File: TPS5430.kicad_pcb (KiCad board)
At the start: 2 copper layers, 55 x 20 mm, 36 parts, among them J1 Barrel_Jack, J2 Screw_Terminal_01x02, Q1 AO3401A, U1 TPS5430DDA

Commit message: Add library with used extra parts
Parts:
- J1: footprint MyFootprints:DC-005-5A-2.0-SMT -> tps5430:DC-005-5A-2.0-SMT
- L1: footprint MyFootprints:L_Sunlord_MWSA1004S_10x11.5x4mm -> tps5430:L_Sunlord_MWSA1004S_10x11.5x4mm
- REF** (x3): footprint MyFootprints:ToolingHole_1.152mm -> tps5430:ToolingHole_1.152mm
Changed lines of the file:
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@@
     )
   )
-  (footprint "MyFootprints:L_Sunlord_MWSA1004S_10x11.5x4mm" (layer "F.Cu")
+  (footprint "tps5430:L_Sunlord_MWSA1004S_10x11.5x4mm" (layer "F.Cu")
     (at 187.4 87.1 90)
     (descr "Inductor, Sunlord, MWSA series, MWSA1004S-470MT, SMD_10x11.5x4.0mm, 47uH ±20% 3.3A 145mΩ SMD,10x11.5x4.0mm Power Inductors RoHS, https://datasheet.lcsc.com/szlcsc/1912111437_Sunlord-MWSA1004S-470MT_C408491.pdf")
@@
     (property "Sheetname" "")
     (attr smd)
-    (fp_text reference "L1" (at -6.3 6 90) (layer "F.SilkS")
-      (effects (font (size 1 1) (thickness 0.15)))
-    )
-    (fp_text value "47u" (at 16.75 -21.8 90) (layer "F.Fab")
+    (fp_text reference "L1" (at 0 -6.25 90) (layer "F.SilkS")
+      (effects (font (size 1 1) (thickness 0.15)))
+    )
+    (fp_text value "47u" (at 0 6.5 90) (layer "F.Fab")
       (effects (font (size 1 1) (thickness 0.15)))
     )
@@
     (fp_line (start -5.15 5.3) (end 5.15 5.3) (layer "F.SilkS") (width 0.12))
     (fp_line (start -5.15 -5.3) (end 5.15 -5.3) (layer "F.SilkS") (width 0.12))
-    (fp_line (start 6.95 -5.3) (end -6.95 -5.3) (layer "F.CrtYd") (width 0.05))
+    (fp_line (start -6.95 5.3) (end 6.95 5.3) (layer "F.CrtYd") (width 0.05))
     (fp_line (start -6.95 -5.3) (end -6.95 5.3) (layer "F.CrtYd") (width 0.05))
     (fp_line (start 6.95 5.3) (end 6.95 -5.3) (layer "F.CrtYd") (width 0.05))
-    (fp_line (start -6.95 5.3) (end 6.95 5.3) (layer "F.CrtYd") (width 0.05))
+    (fp_line (start 6.95 -5.3) (end -6.95 -5.3) (layer "F.CrtYd") (width 0.05))
+    (fp_line (start 5.75 5) (end 5.75 -5) (layer "F.Fab") (width 0.1))
+    (fp_line (start -5.75 -5) (end -5.75 5) (layer "F.Fab") (width 0.1))
     (fp_line (start 5.75 -5) (end -5.75 -5) (layer "F.Fab") (width 0.1))
     (fp_line (start -5.75 5) (end 5.75 5) (layer "F.Fab") (width 0.1))
-    (fp_line (start 5.75 5) (end 5.75 -5) (layer "F.Fab") (width 0.1))
-    (fp_line (start -5.75 -5) (end -5.75 5) (layer "F.Fab") (width 0.1))
     (pad "1" smd rect locked (at -4.75 0 90) (size 4.1 4.1) (layers "F.Cu" "F.Paste" "F.Mask" "Eco2.User")
       (net 5 "Net-(C6-Pad2)") (pinfunction "1") (pintype "passive"))
     (pad "2" smd rect locked (at 4.75 0 90) (size 4.1 4.1) (layers "F.Cu" "F.Paste" "F.Mask")
       (net 6 "VDD") (pinfunction "2") (pintype "passive"))
-    (model "${KICAD_USER_3DMODEL_DIR}/MWSA1004S-150MT.stp"
+    (model "${KIPRJMOD}/lib/3dmodels/MWSA1004S-150MT.stp"
       (offset (xyz 0 0 0))
       (scale (xyz 1 1 1))
@@
     )
   )
-  (footprint "MyFootprints:ToolingHole_1.152mm" (layer "F.Cu")
+  (footprint "tps5430:ToolingHole_1.152mm" (layer "F.Cu")
     (at 152.75 77.5)
     (descr "Mounting Hole 1.152mm, no annular")
@@
     (pad "1" np_thru_hole circle locked (at 0 0) (size 2.2 2.2) (drill 2.2) (layers *.Cu *.Mask))
   )
-  (footprint "MyFootprints:ToolingHole_1.152mm" (layer "F.Cu")
+  (footprint "tps5430:ToolingHole_1.152mm" (layer "F.Cu")
     (at 196.25 77.5)
     (descr "Mounting Hole 1.152mm, no annular")
@@
     )
   )
-  (footprint "MyFootprints:ToolingHole_1.152mm" (layer "F.Cu")
+  (footprint "tps5430:ToolingHole_1.152mm" (layer "F.Cu")
     (at 196.25 94.5)
     (descr "Mounting Hole 1.152mm, no annular")
@@
     )
   )
-  (footprint "MyFootprints:DC-005-5A-2.0-SMT" (layer "F.Cu")
+  (footprint "tps5430:DC-005-5A-2.0-SMT" (layer "F.Cu")
     (at 154.3 86)
     (descr "XKB Barrel Jack Connector, 2.5A, 2.0mm pin, 2.1mm/5.5mm plug, DC-005-5A-2.0-SMT-1, https://datasheet.lcsc.com/szlcsc/1810291122_XKB-Connectivity-DC-005-5A-2-0-SMT_C319134.pdf")
@@
     (property "Sheetfile" "TPS5430.kicad_sch")
     (property "Sheetname" "")
-    (fp_text reference "J1" (at 6.7 -8.5) (layer "F.SilkS")
+    (fp_text reference "J1" (at 0 0) (layer "F.SilkS")
       (effects (font (size 1.27 1.27) (thickness 0.254)))
     )
@@
       (effects (font (size 1.27 1.27) (thickness 0.254)))
     )
-    (fp_line (start 7.4 4.5) (end 6.1 4.5) (layer "F.SilkS") (width 0.1))
+    (fp_line (start -4.15 4.56) (end -4.15 -4.56) (layer "F.SilkS") (width 0.12))
+    (fp_line (start 6.1 -4.5) (end 7.4 -4.5) (layer "F.SilkS") (width 0.1))
+    (fp_line (start -4.15 -3) (end 0.65 -3) (layer "F.SilkS") (width 0.12))
     (fp_line (start -7.4 -4.5) (end -7.4 4.5) (layer "F.SilkS") (width 0.1))
-    (fp_line (start -4.15 -3) (end 0.65 -3) (layer "F.SilkS") (width 0.12))
-    (fp_line (start -0.4 4.5) (end 1.6 4.5) (layer "F.SilkS") (width 0.1))
-    (fp_line (start -4.15 4.56) (end -4.15 -4.56) (layer "F.SilkS") (width 0.12))
-    (fp_line (start -0.4 -4.5) (end 1.6 -4.5) (layer "F.SilkS") (width 0.1))
-    (fp_line (start 6.1 -4.5) (end 7.4 -4.5) (layer "F.SilkS") (width 0.1))
-    (fp_line (start -7.4 4.5) (end -4.9 4.5) (layer "F.SilkS") (width 0.1))
-    (fp_line (start 7.4 -4.5) (end 7.4 4.5) (layer "F.SilkS") (width 0.1))
     (fp_line (start -4.15 3) (end 0.65 3) (layer "F.SilkS") (width 0.12))
     (fp_line (start -4.9 -4.5) (end -7.4 -4.5) (layer "F.SilkS") (width 0.1))
+    (fp_line (start 7.4 4.5) (end 6.1 4.5) (layer "F.SilkS") (width 0.1))
+    (fp_line (start -0.4 -4.5) (end 1.6 -4.5) (layer "F.SilkS") (width 0.1))
+    (fp_line (start 7.4 -4.5) (end 7.4 4.5) (layer "F.SilkS") (width 0.1))
+    (fp_line (start -7.4 4.5) (end -4.9 4.5) (layer "F.SilkS") (width 0.1))
+    (fp_line (start -0.4 4.5) (end 1.6 4.5) (layer "F.SilkS") (width 0.1))
     (fp_arc (start 0.65 0) (end 0.65 3) (angle -180) (layer "F.SilkS") (width 0.12))
     (fp_line (start 7.9 7.4) (end -7.9 7.4) (layer "F.CrtYd") (width 0.1))
     (fp_line (start -7.9 -7.4) (end 7.9 -7.4) (layer "F.CrtYd") (width 0.1))
+    (fp_line (start 7.9 -7.4) (end 7.9 7.4) (layer "F.CrtYd") (width 0.1))
     (fp_line (start -7.9 7.4) (end -7.9 -7.4) (layer "F.CrtYd") (width 0.1))
-    (fp_line (start 7.9 -7.4) (end 7.9 7.4) (layer "F.CrtYd") (width 0.1))
+    (fp_line (start 7.4 4.5) (end -7.4 4.5) (layer "F.Fab") (width 0.2))
     (fp_line (start 7.4 -4.5) (end 7.4 4.5) (layer "F.Fab") (width 0.2))
+    (fp_line (start -7.4 -4.5) (end 7.4 -4.5) (layer "F.Fab") (width 0.2))
     (fp_line (start -7.4 4.5) (end -7.4 -4.5) (layer "F.Fab") (width 0.2))
-    (fp_line (start -7.4 -4.5) (end 7.4 -4.5) (layer "F.Fab") (width 0.2))
-    (fp_line (start 7.4 4.5) (end -7.4 4.5) (layer "F.Fab") (width 0.2))
     (pad "1" smd rect (at 3.7 -5.7 90) (size 2.4 2.8) (layers "F.Cu" "F.Paste" "F.Mask")
       (net 8 "Net-(F1-Pad1)") (pintype "passive"))
@@
     (pad "MH1" np_thru_hole circle (at -2.4 0) (size 1.6 1.6) (drill 1.6) (layers *.Cu *.Mask))
     (pad "MH2" np_thru_hole circle (at 2.1 0) (size 1.8 1.8) (drill 1.8) (layers *.Cu *.Mask))
-    (model "${KICAD_USER_3DMODEL_DIR}/DC-005-5A-2.0-SMT.stp"
-      (offset (xyz 0 0 0))
-      (scale (xyz 1 1 1))
+    (model "${KIPRJMOD}/lib/3dmodels/DC-005-5A-2.0-SMT.stp"
+      (offset (xyz 0 0 0))
+      (scale (xyz 1 1 1))

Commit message: Add License notice in files and on the PCB
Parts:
- added LOGO1: Logo_Open_Hardware_Small, Symbol:OSHW-Logo_11.4x12mm_Copper, B.Cu at (154.8, 86.0)
- added REF**: KiCad-Logo2_5mm_Copper, Symbol:KiCad-Logo2_5mm_Copper, B.Cu at (191.5, 86.0)
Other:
- board text added: "git.io/JWgnY"

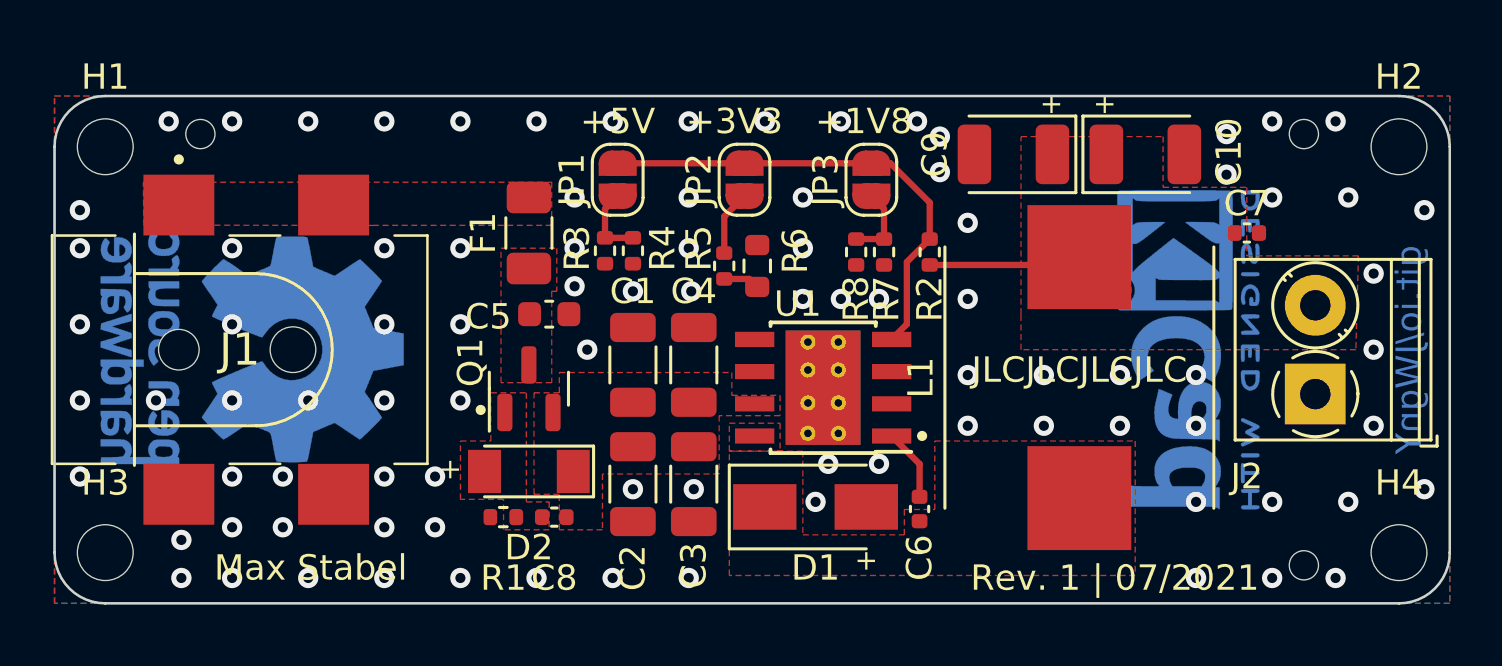
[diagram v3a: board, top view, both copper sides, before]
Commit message: Add TP & 12V SolderJumper
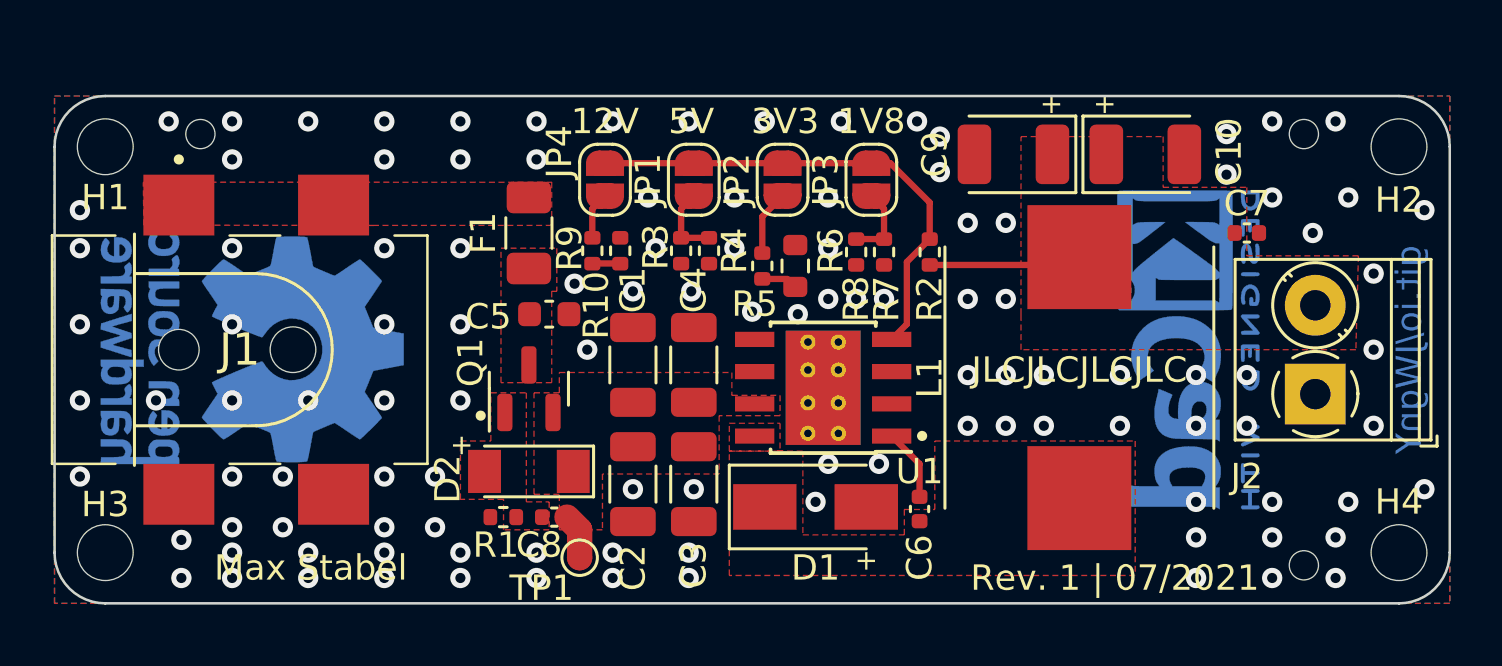
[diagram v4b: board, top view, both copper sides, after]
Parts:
- added JP4: SolderJumper, Jumper:SolderJumper-2_P1.3mm_Open_RoundedPad1.0x1.5mm, F.Cu at (168.7, 79.3)
- added R10: 120, Resistor_SMD:R_0402_1005Metric, F.Cu at (169.3, 82.1)
- added R9: 1k, Resistor_SMD:R_0402_1005Metric, F.Cu at (168.2, 82.1)
- added TP1: TestPoint, TestPoint:TestPoint_Pad_D1.0mm, F.Cu at (167.7, 94.2)
- JP1, JP2, JP3: value SolderJumper_2_Open -> SolderJumper
- moved JP1 3.00 mm to (172.2, 79.3)
- moved R3 3.00 mm to (171.7, 82.1)
- moved R4 3.00 mm to (172.8, 82.1)
- moved JP2 1.50 mm to (175.7, 79.3)
- moved R5 1.50 mm to (174.9, 82.7)
- moved R6 1.50 mm to (176.2, 82.7)
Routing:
- net VCC: track 0.00 -> 1.81 mm
- net Net-(JP4-Pad1): track 0.00 -> 1.75 mm
- net Net-(R10-Pad1): track 0.00 -> 1.17 mm
- net GND: vias 91 -> 114
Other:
- board text added: "12V"
- board text added: "1V8"
- board text added: "3V3"
- board text added: "5V"
- board text added: "M2 Screw"
- board text removed: "+1V8"
- board text removed: "+3V3"
- board text removed: "+5V"

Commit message: Add Status LED
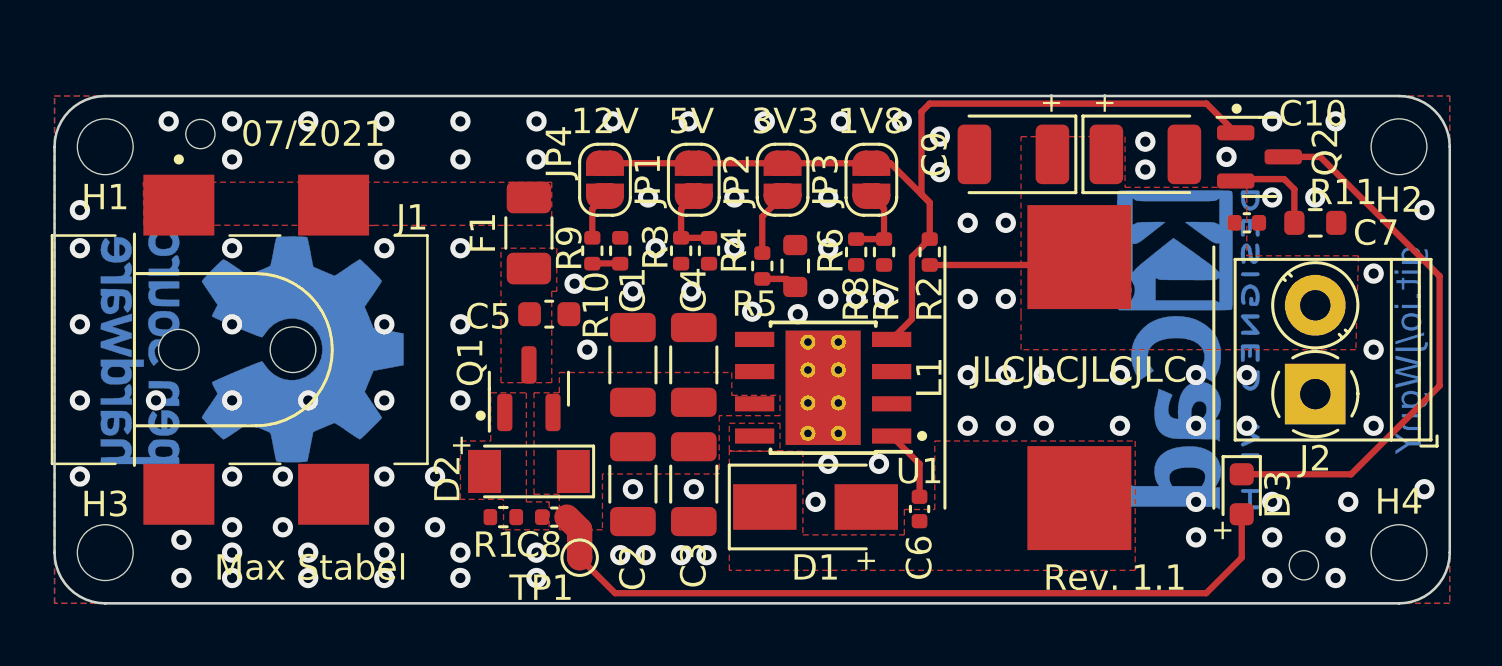
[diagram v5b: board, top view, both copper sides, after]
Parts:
- removed the REF** at (196.2, 77.5)
- added D3: LED, LED_SMD:LED_0603_1608Metric, F.Cu at (193.8, 91.7)
- added Q2: MMBT3904, Package_TO_SOT_SMD:SOT-23, F.Cu at (194.5, 78.4)
- added R11: 270, Resistor_SMD:R_0603_1608Metric, F.Cu at (196.7, 81.0)
- moved C7 0.40 mm to (194.0, 81.0)
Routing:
- net VCC: track 1.81 -> 30.8 mm
- net Net-(D3-Pad1): track 0.00 -> 21.7 mm
- net /Feedback: track 19.0 -> 35.7 mm
- net Net-(Q2-Pad2): track 0.00 -> 3.83 mm
- net GND: vias 114 -> 113
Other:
- board text added: "07/2021"
- board text added: "Rev. 1.1"
- board text removed: "Rev. 1 | 07/2021"

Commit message: Add status LED & fix reverse polarity protection
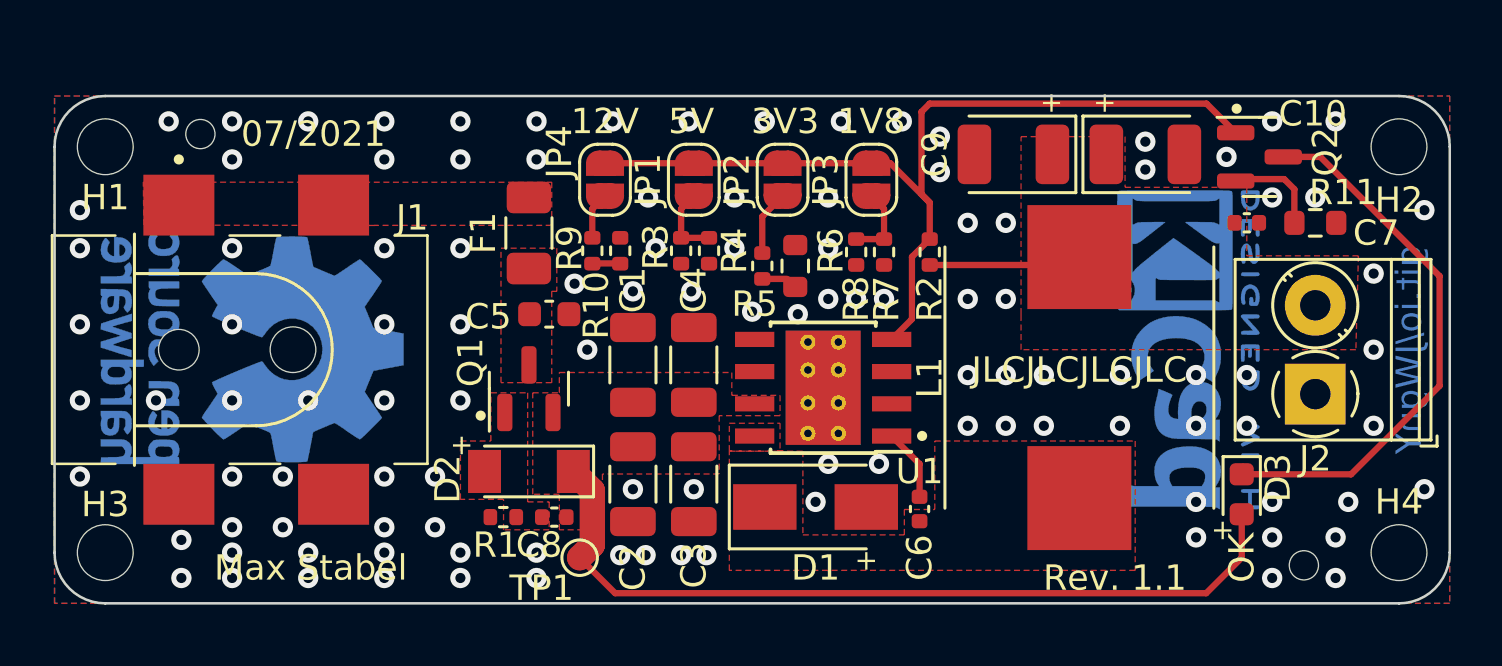
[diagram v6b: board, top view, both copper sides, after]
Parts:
- C8: value 100n/16V -> 4n7/50V
- R1: value 12k -> 100k
- turned C8 to 0 degrees
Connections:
- C8 pad 1: VCC -> Net-(R1-Pad1)
- C8 pad 2: Net-(C8-Pad2) -> GND
- D2 pad 2: Net-(C8-Pad2) -> Net-(R1-Pad1)
- Q1 pad 1: Net-(C8-Pad2) -> Net-(R1-Pad1)
- R1 pad 1: Net-(C8-Pad2) -> Net-(R1-Pad1)
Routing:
- net VCC: track 30.8 -> 32.9 mm
- added copper zone on F.Cu, net Net-(R1-Pad1)
- removed copper zone on F.Cu, net Net-(C8-Pad2)
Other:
- board text added: "OK"

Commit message: Dim status LED and update to KiCAD 6
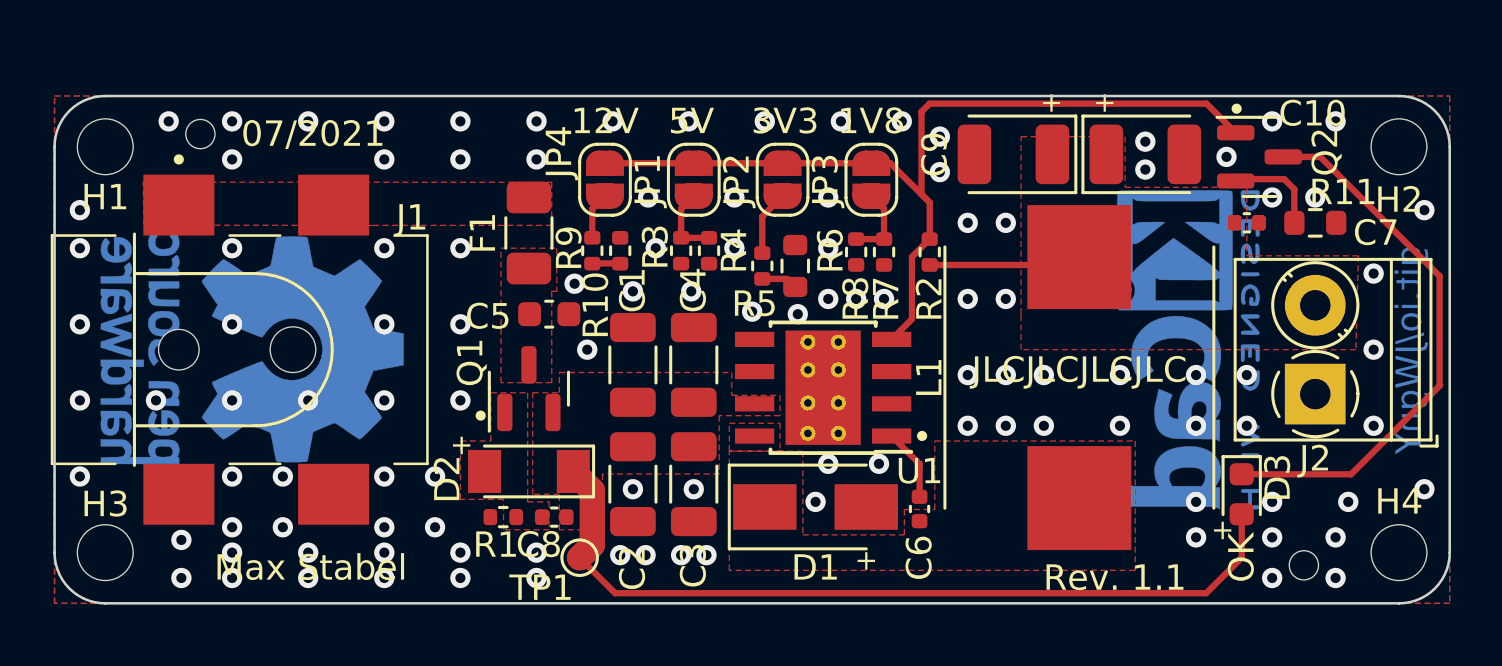
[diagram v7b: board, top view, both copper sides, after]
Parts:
- C10, C9: value 100u/6.3V -> 100u/6.3V
- C5: value 100n/50V -> 100n/50V
- C8: value 4n7/50V -> 4n7/50V
- R11: value 270 -> 10k
